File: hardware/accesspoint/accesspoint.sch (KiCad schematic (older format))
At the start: 27 parts

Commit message: fixed schematic, made netlist and more
associated footprints with parts
made a board (but didn't place parts or make traces)

a lot of lessons learned
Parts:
- removed D? (x2): LED, symbol LED
- removed Q? (x4): Q_NPN_BCE, symbol Q_NPN_BCE
- removed Q?: Q_NMOS_GDS, symbol Q_NMOS_GDS
- removed R? (x2): R220, symbol R
- removed SP?: SPEAKER, symbol SPEAKER
- removed U?: Teensy_3.0, symbol Teensy_3.0
- removed U?: RDM6300, symbol RDM6300
- added P1, P2: CONN_2, Connect:PINHEAD1-2, symbol CONN_2
- added P3, P4: CONN_8, Connect:RJ45_8, symbol CONN_8
- added Q?: MOS_N, symbol MOS_N
- added Q?: NPN, symbol NPN
- added U4: Teensy_3.0, myLib:Teensy3.1, symbol Teensy_3.0
- C1, C2, C3: renamed from C?; footprint (none) -> Discret:C1
- D1: renamed from D?; footprint (none) -> LEDs:LED-5MM
- R1, R2, R3, R4, R5, R6, R7: renamed from R?; footprint (none) -> Discret:R3
- U1, U2, U3: renamed from U?; footprint TO-220 -> Power_Integrations:TO-220
- U5: renamed from U?; footprint (none) -> myLib:Teensy3.1
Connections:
- net labels added: +3V3
- net labels removed: +12V, Buzzer, Door_Lock, Ethernet_Jack_1, Ethernet_Jack_2, KeyPad, LED1, LED2, Ret, RxD, Spare
- wire segments 148 -> 83
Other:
- moved on the sheet: C1, C2, C3, D1, R1, R2, R3, R4, R5, R6, R7, U1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

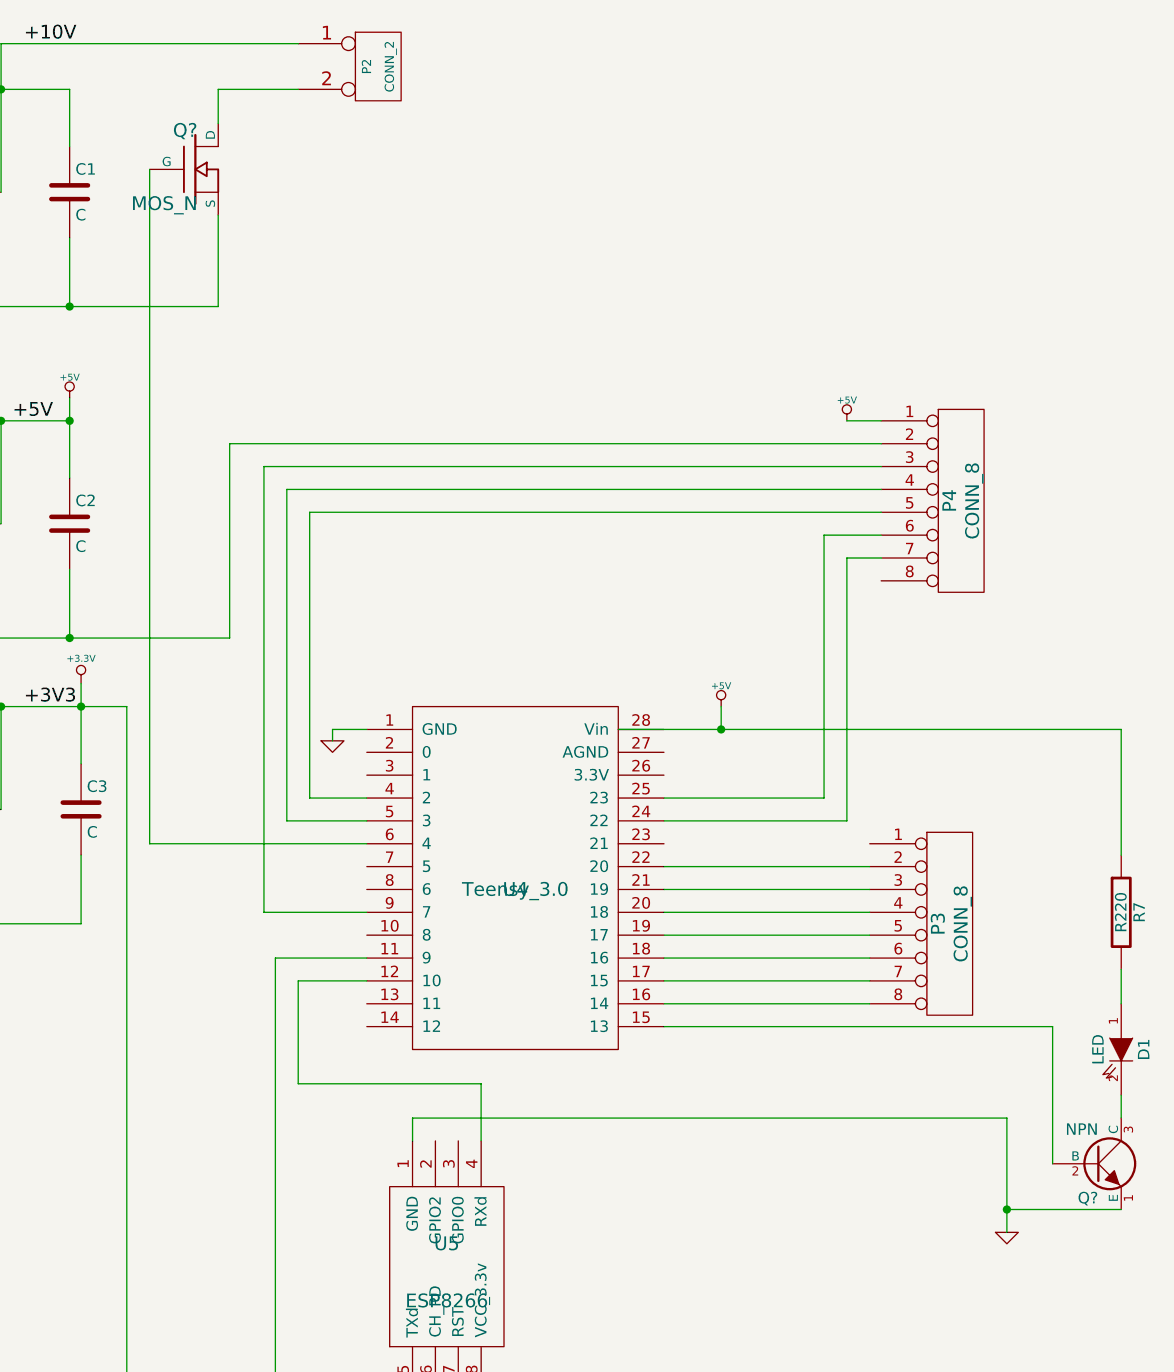
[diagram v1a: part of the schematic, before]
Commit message: fixed board and generated top/bottom pcbs
for some reason the files do not load correctly in kicad but works locally
top and bottom pdfs are generated here with silks
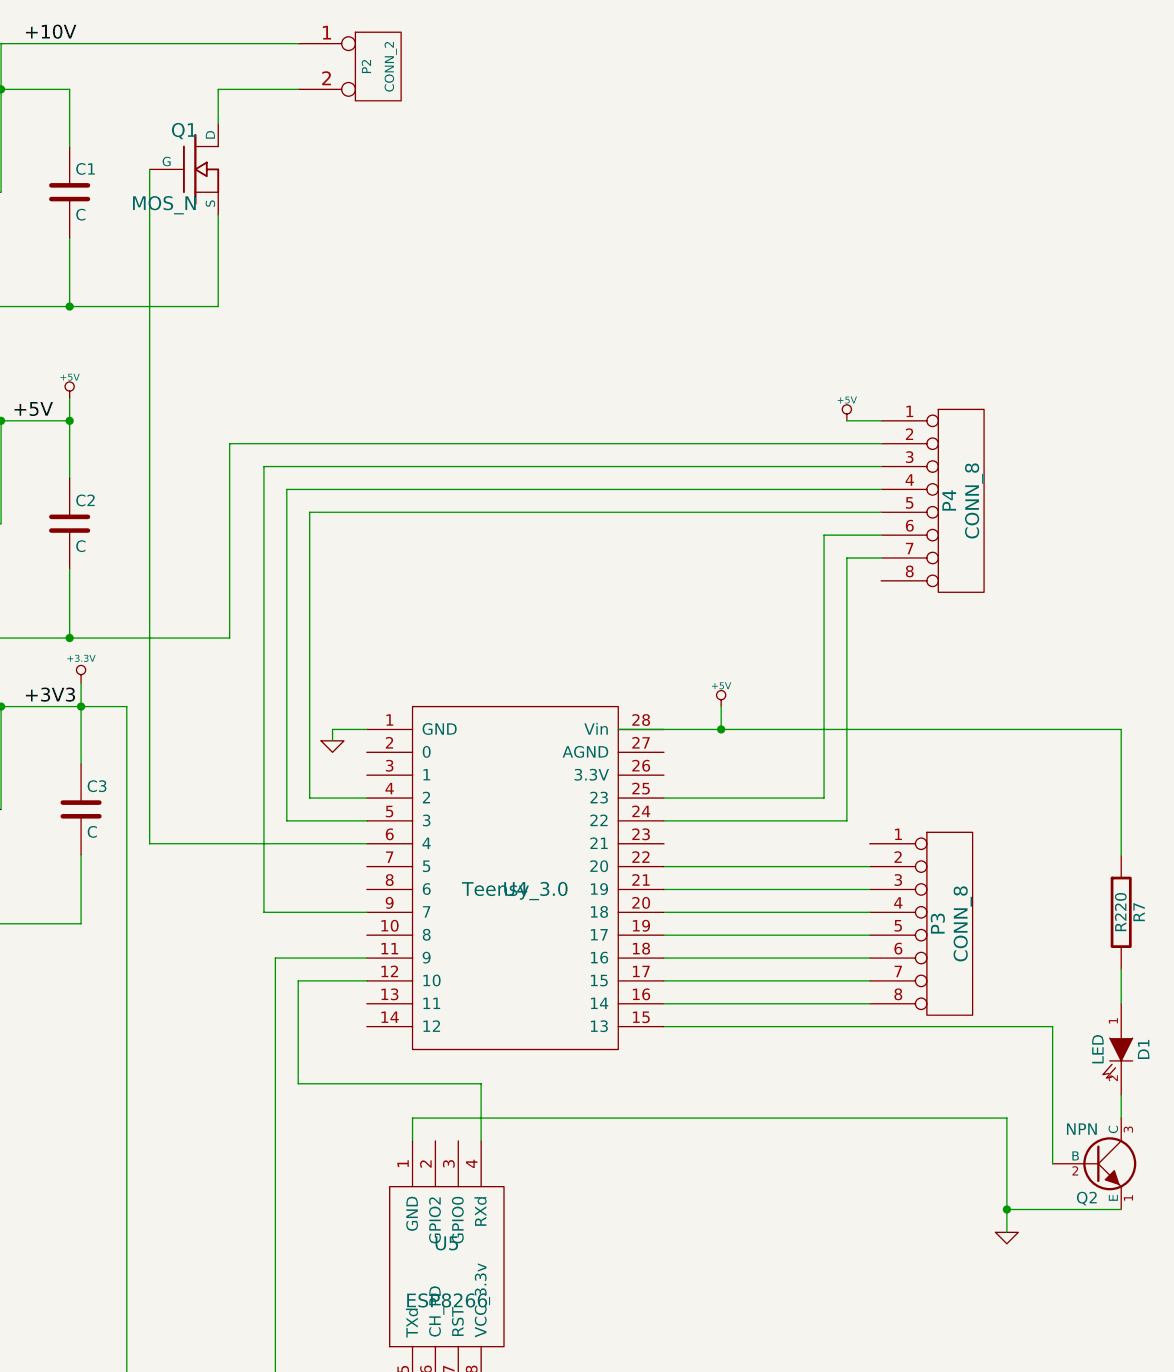
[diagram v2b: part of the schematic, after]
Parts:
- gave numbers to parts that had none: 2
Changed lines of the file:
@@
 LIBS:accesspoint_library
 LIBS:valves
+LIBS:accesspoint-cache
 EELAYER 24 0
 EELAYER END
@@
 	6100 3000 6250 3000
 $Comp
-L +3.3V #PWR01
+L +3.3V #PWR3
 U 1 1 5525DC38
 P 2750 3550
-F 0 "#PWR01" H 2750 3510 30  0001 C CNN
+F 0 "#PWR3" H 2750 3510 30  0001 C CNN
 F 1 "+3.3V" H 2750 3660 30  0000 C CNN
 F 2 "" H 2750 3550 60  0000 C CNN
@@
 $EndComp
 $Comp
-L +5V #PWR02
+L +5V #PWR2
 U 1 1 5525DC4C
 P 2700 2300
-F 0 "#PWR02" H 2700 2390 20  0001 C CNN
+F 0 "#PWR2" H 2700 2390 20  0001 C CNN
 F 1 "+5V" H 2700 2390 30  0000 C CNN
 F 2 "" H 2700 2300 60  0000 C CNN
@@
 	2150 2400 2700 2400
 $Comp
-L +5V #PWR03
+L +5V #PWR6
 U 1 1 5525E338
 P 6100 2400
-F 0 "#PWR03" H 6100 2490 20  0001 C CNN
+F 0 "#PWR6" H 6100 2490 20  0001 C CNN
 F 1 "+5V" H 6100 2490 30  0000 C CNN
 F 2 "" H 6100 2400 60  0000 C CNN
@@
 	6100 2400 6250 2400
 $Comp
-L +5V #PWR04
+L +5V #PWR5
 U 1 1 5525E4F1
 P 5550 3650
-F 0 "#PWR04" H 5550 3740 20  0001 C CNN
+F 0 "#PWR5" H 5550 3740 20  0001 C CNN
 F 1 "+5V" H 5550 3740 30  0000 C CNN
 F 2 "" H 5550 3650 60  0000 C CNN
@@
 	5550 3650 5550 3750
 $Comp
-L GND #PWR05
+L GND #PWR1
 U 1 1 5525E6AD
 P 1750 4750
-F 0 "#PWR05" H 1750 4750 30  0001 C CNN
+F 0 "#PWR1" H 1750 4750 30  0001 C CNN
 F 1 "GND" H 1750 4680 30  0001 C CNN
 F 2 "" H 1750 4750 60  0000 C CNN
@@
 $EndComp
 $Comp
-L GND #PWR06
+L GND #PWR4
 U 1 1 5525E8A2
 P 3850 3800
-F 0 "#PWR06" H 3850 3800 30  0001 C CNN
+F 0 "#PWR4" H 3850 3800 30  0001 C CNN
 F 1 "GND" H 3850 3730 30  0001 C CNN
 F 2 "" H 3850 3800 60  0000 C CNN
@@
 	3850 3750 4000 3750
 $Comp
-L GND #PWR07
+L GND #PWR7
 U 1 1 5525EC44
 P 6800 5950
-F 0 "#PWR07" H 6800 5950 30  0001 C CNN
+F 0 "#PWR7" H 6800 5950 30  0001 C CNN
 F 1 "GND" H 6800 5880 30  0001 C CNN
 F 2 "" H 6800 5950 60  0000 C CNN
@@
 	2750 4600 2750 4300
 $Comp
-L MOS_N Q?
+L MOS_N Q1
 U 1 1 5525E05A
 P 3250 1300
-F 0 "Q?" H 3260 1470 60  0000 R CNN
+F 0 "Q1" H 3260 1470 60  0000 R CNN
 F 1 "MOS_N" H 3260 1150 60  0000 R CNN
 F 2 "" H 3250 1300 60  0000 C CNN
@@
 $EndComp
 $Comp
-L NPN Q?
+L NPN Q2
 U 1 1 5525E2BB
 P 7200 5650
-F 0 "Q?" H 7200 5500 50  0000 R CNN
+F 0 "Q2" H 7200 5500 50  0000 R CNN
 F 1 "NPN" H 7200 5800 50  0000 R CNN
 F 2 "" H 7200 5650 60  0000 C CNN
